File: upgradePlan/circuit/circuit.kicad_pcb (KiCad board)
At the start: 2 copper layers, 3 parts, among them U2 L293D, U3 LM317_TO-220, U5 LM317_TO-220

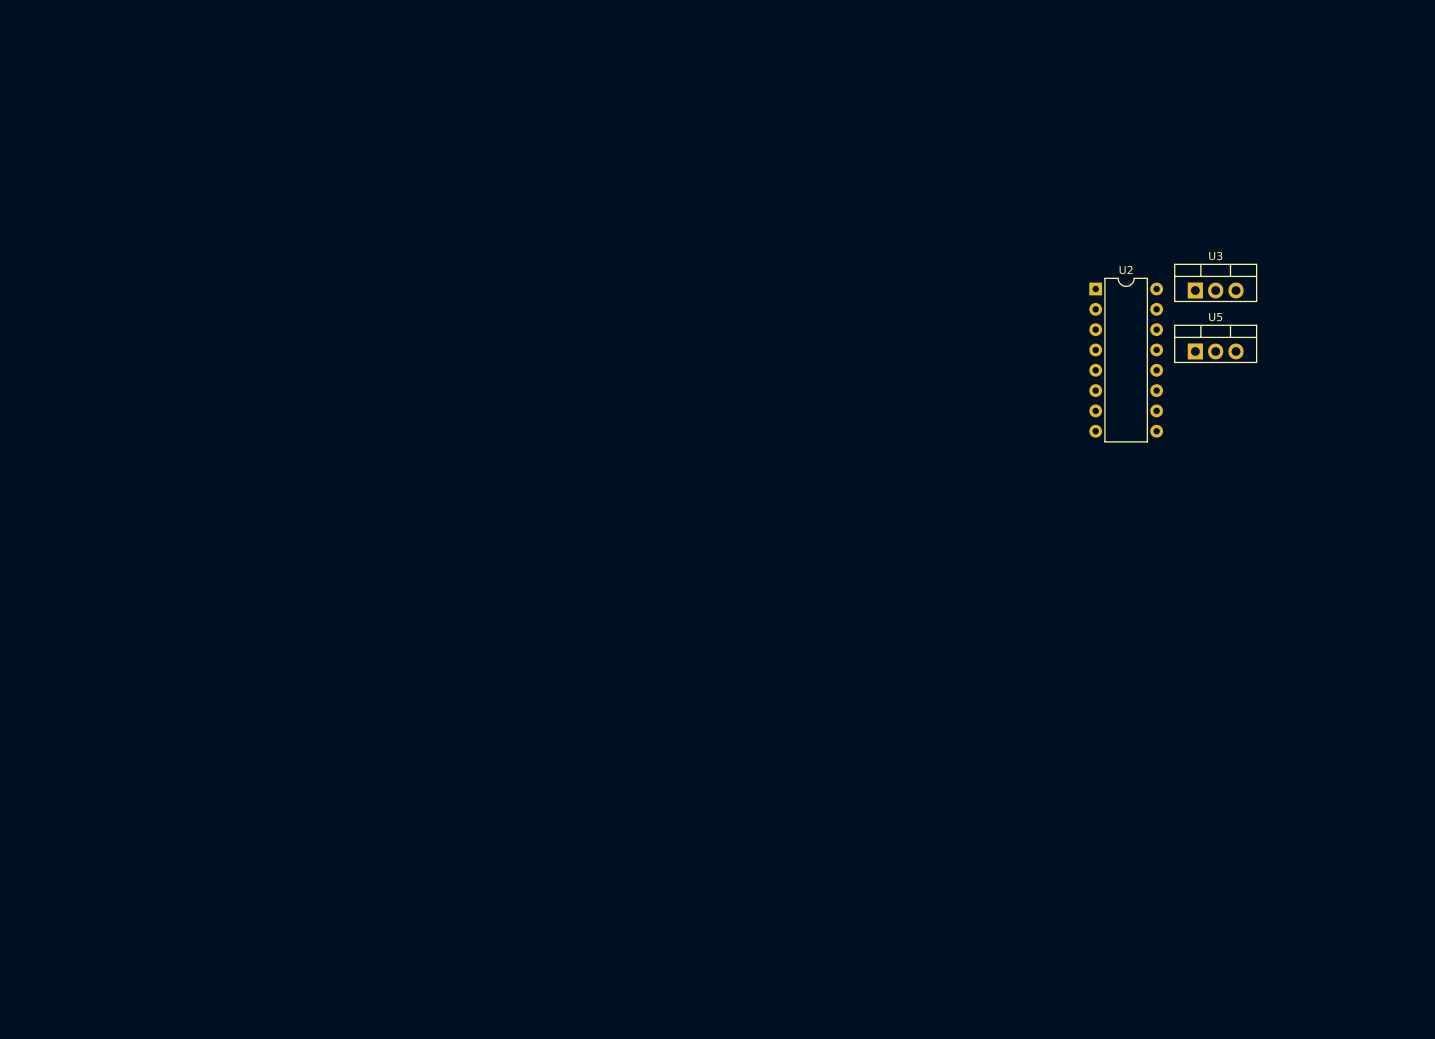
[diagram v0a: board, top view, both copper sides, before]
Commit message: added footprints to schematic and board edge
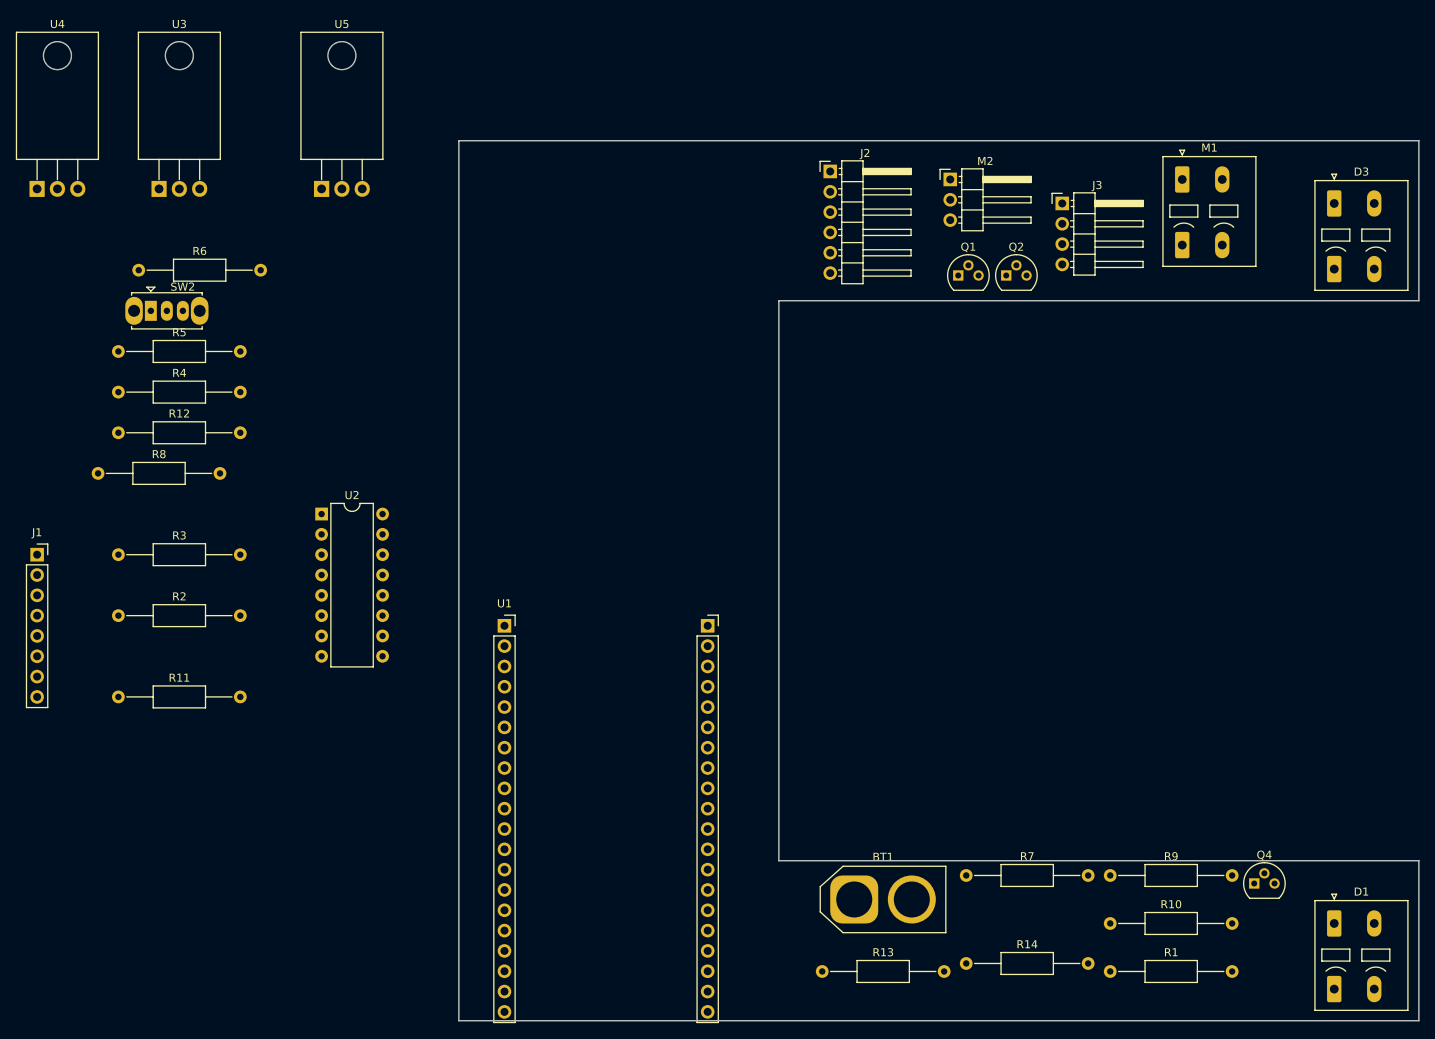
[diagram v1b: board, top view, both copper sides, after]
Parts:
- added BT1: Battery_Cell, Connector_AMASS:AMASS_XT60-M_1x02_P7.20mm_Vertical, F.Cu at (125.0, 132.0)
- added D1: LED, Connector_Phoenix_SPT:PhoenixContact_SPT_2.5_2-V-5.0-EX_1x02_P5.0mm_Vertical, F.Cu at (185.0, 135.0)
- added D3: LED, Connector_Phoenix_SPT:PhoenixContact_SPT_2.5_2-V-5.0-EX_1x02_P5.0mm_Vertical, F.Cu at (185.0, 45.0)
- added J1: Connector_GY_521, Connector_PinSocket_2.54mm:PinSocket_1x08_P2.54mm_Vertical, F.Cu at (22.9, 88.9)
- added J2: Conn_VL53L0/1xV2, Connector_PinHeader_2.54mm:PinHeader_1x06_P2.54mm_Horizontal, F.Cu at (122.0, 41.0)
- added J3: Conn_HC_SR04, Connector_PinHeader_2.54mm:PinHeader_1x04_P2.54mm_Horizontal, F.Cu at (151.0, 45.0)
- added M1: Motor_DC, Connector_Phoenix_SPT:PhoenixContact_SPT_2.5_2-V-5.0-EX_1x02_P5.0mm_Vertical, F.Cu at (166.0, 42.0)
- added M2: Motor_Servo, Connector_PinHeader_2.54mm:PinHeader_1x03_P2.54mm_Horizontal, F.Cu at (137.0, 42.0)
- added Q1: C945, Package_TO_SOT_THT:TO-92, F.Cu at (138.0, 54.0)
- added Q2: C945, Package_TO_SOT_THT:TO-92, F.Cu at (144.0, 54.0)
- added Q4: C945, Package_TO_SOT_THT:TO-92, F.Cu at (175.0, 130.0)
- added R1: 390, Resistor_THT:R_Axial_DIN0207_L6.3mm_D2.5mm_P15.24mm_Horizontal, F.Cu at (157.0, 141.0)
- added R10: 4k7, Resistor_THT:R_Axial_DIN0207_L6.3mm_D2.5mm_P15.24mm_Horizontal, F.Cu at (157.0, 135.0)
- added R11: 3k, Resistor_THT:R_Axial_DIN0207_L6.3mm_D2.5mm_P15.24mm_Horizontal, F.Cu at (33.0, 106.7)
- added R12: 100k, Resistor_THT:R_Axial_DIN0207_L6.3mm_D2.5mm_P15.24mm_Horizontal, F.Cu at (33.0, 73.7)
- added R13: 120, Resistor_THT:R_Axial_DIN0207_L6.3mm_D2.5mm_P15.24mm_Horizontal, F.Cu at (121.0, 141.0)
- added R14: 510, Resistor_THT:R_Axial_DIN0207_L6.3mm_D2.5mm_P15.24mm_Horizontal, F.Cu at (139.0, 140.0)
- added R2: 3k, Resistor_THT:R_Axial_DIN0207_L6.3mm_D2.5mm_P15.24mm_Horizontal, F.Cu at (33.0, 96.5)
- added R3: 220, Resistor_THT:R_Axial_DIN0207_L6.3mm_D2.5mm_P15.24mm_Horizontal, F.Cu at (33.0, 88.9)
- added R4: 220, Resistor_THT:R_Axial_DIN0207_L6.3mm_D2.5mm_P15.24mm_Horizontal, F.Cu at (33.0, 68.6)
- added R5: 1k, Resistor_THT:R_Axial_DIN0207_L6.3mm_D2.5mm_P15.24mm_Horizontal, F.Cu at (33.0, 63.5)
- added R6: 1k, Resistor_THT:R_Axial_DIN0207_L6.3mm_D2.5mm_P15.24mm_Horizontal, F.Cu at (35.6, 53.3)
- added R7: 39, Resistor_THT:R_Axial_DIN0207_L6.3mm_D2.5mm_P15.24mm_Horizontal, F.Cu at (139.0, 129.0)
- added R8: 120, Resistor_THT:R_Axial_DIN0207_L6.3mm_D2.5mm_P15.24mm_Horizontal, F.Cu at (30.5, 78.7)
- added R9: 4k7, Resistor_THT:R_Axial_DIN0207_L6.3mm_D2.5mm_P15.24mm_Horizontal, F.Cu at (157.0, 129.0)
- added SW2: SW_DPDT_x2, Button_Switch_THT:SW_Slide_1P2T_CK_OS102011MS2Q, F.Cu at (37.1, 58.4)
- added U1: Freenove-SP32-WROVER, MyESPConnector:MyESPConnector, F.Cu at (81.3, 97.8)
- added U4: LM350_TO220, Package_TO_SOT_THT:TO-220-3_Horizontal_TabDown, F.Cu at (22.9, 43.2)
- U3: value LM317_TO-220 -> LM350_TO220; footprint Package_TO_SOT_THT:TO-220-3_Vertical -> Package_TO_SOT_THT:TO-220-3_Horizontal_TabDown
- U5: footprint Package_TO_SOT_THT:TO-220-3_Vertical -> Package_TO_SOT_THT:TO-220-3_Horizontal_TabDown
- moved U3 130.2 mm to (38.1, 43.2)
- moved U5 111.1 mm to (58.4, 43.2)
- moved U2 100.8 mm to (58.4, 83.8)
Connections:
- U3 pad 3: Net-(U3-VI) -> /Drive Motor
- U5 pad 3: Net-(U3-VI) -> Net-(SW2A-B)
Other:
- board outline added: 120 x 110 mm

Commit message: added layout of footprints
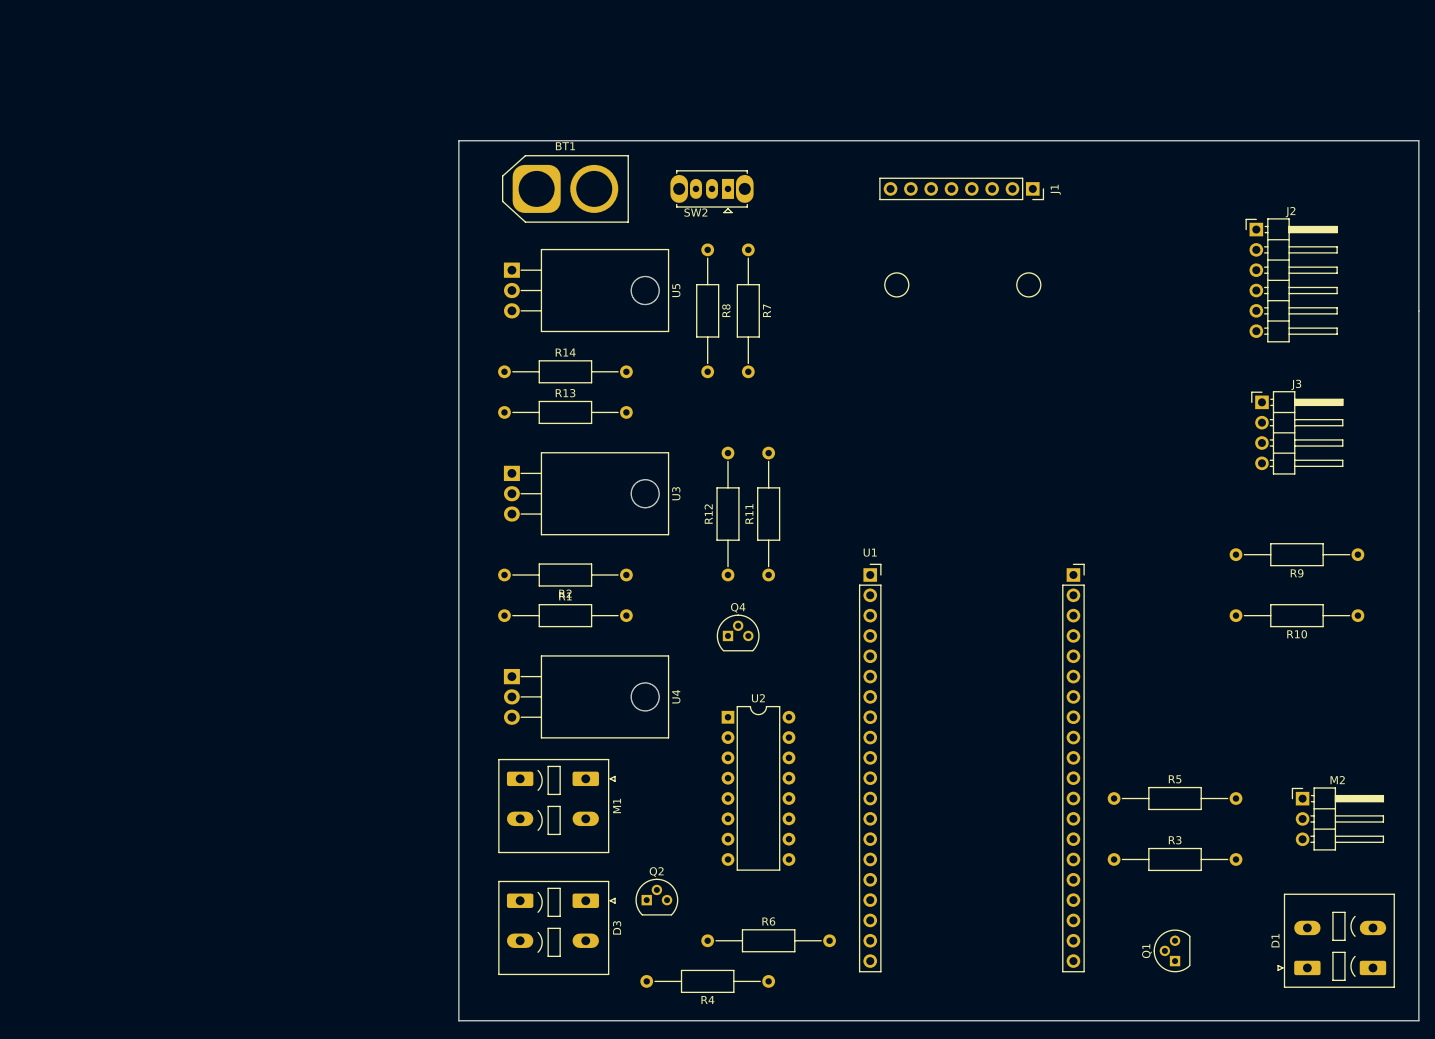
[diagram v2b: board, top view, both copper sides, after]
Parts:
- moved R5 136.4 mm to (157.5, 119.4)
- moved J1 132.6 mm to (147.3, 43.2), turned to -90 degrees
- moved R3 130.2 mm to (157.5, 127.0)
- moved D3 127.9 mm to (91.4, 132.2), turned to -90 degrees
- moved R6 109.9 mm to (106.7, 137.2)
- moved R4 109.7 mm to (114.3, 142.2), turned to 180 degrees
- moved M1 105.7 mm to (91.4, 116.9), turned to -90 degrees
- moved BT1 97.3 mm to (85.3, 43.2)
- moved R14 93.8 mm to (81.3, 66.0)
- moved Q2 90.1 mm to (99.1, 132.1)
- moved Q1 89.9 mm to (165.1, 139.7), turned to 90 degrees
- moved M2 89.1 mm to (181.0, 119.4)
- moved R1 87.8 mm to (81.3, 96.5)
- moved U4 85.1 mm to (82.2, 104.1), turned to -90 degrees
- moved R7 82.8 mm to (111.8, 50.8), turned to -90 degrees
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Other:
- outline, holes or cut-outs redrawn

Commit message: added front routing with auto completed back
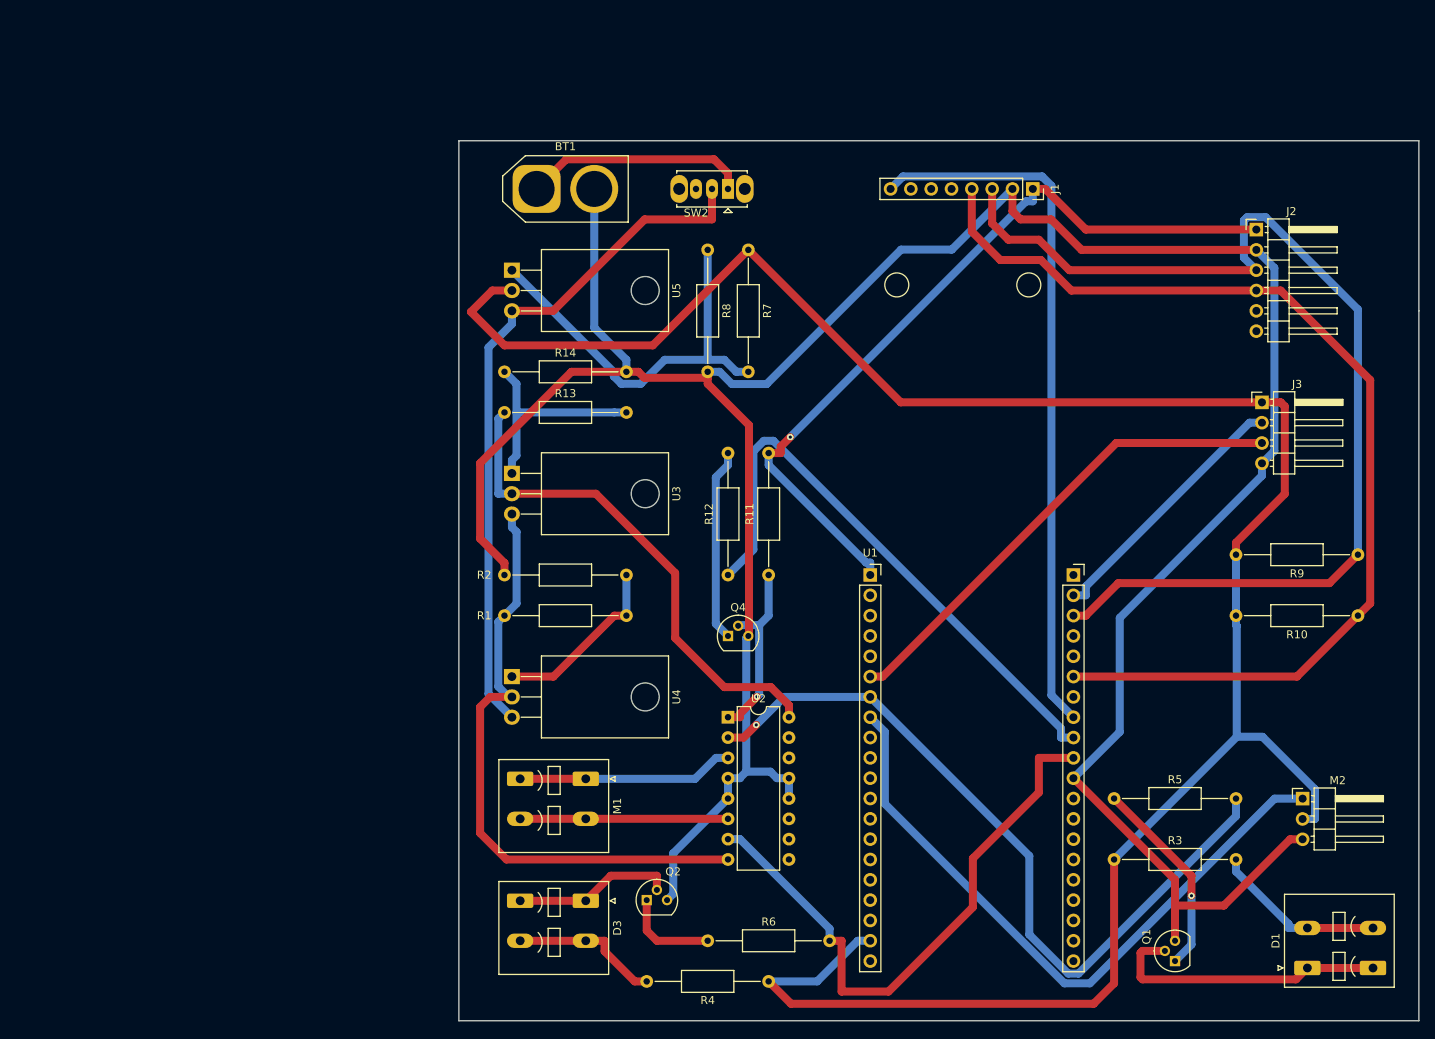
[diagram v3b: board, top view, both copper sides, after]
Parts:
- J1: footprint Connector_PinSocket_2.54mm:PinSocket_1x08_P2.54mm_Vertical -> MyESPConnector:GY-521
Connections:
- R1 pad 1: /Drive Motor -> /MotorDrive
- R13 pad 1: /Drive Motor -> /DriverPower
- U2 pad 12: unconnected-(U2-GND-Pad12) -> GND
- U2 pad 13: unconnected-(U2-GND-Pad13) -> GND
- U2 pad 16: /Drive Motor -> /DriverPower
- U2 pad 5: unconnected-(U2-GND-Pad5) -> GND
- U2 pad 8: /Drive Motor -> /MotorDrive
- U3 pad 2: /Drive Motor -> /DriverPower
- U3 pad 3: /Drive Motor -> /MotorDrive
- U4 pad 2: /Drive Motor -> /MotorDrive
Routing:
- net GND: track 0.00 -> 361.2 mm
- net /ESP Power: track 0.00 -> 281.7 mm
- net Net-(J1-SCL): track 0.00 -> 135.2 mm
- net Net-(J1-SDA): track 0.00 -> 131.6 mm
- net Net-(J1-VCC): track 0.00 -> 98.9 mm, vias 0 -> 1
- net Net-(U1-32): track 0.00 -> 96.0 mm, vias 0 -> 1
- net Net-(J1-INT): track 0.00 -> 88.8 mm
- net Net-(SW2A-B): track 0.00 -> 86.8 mm
- net Net-(M2-PWM): track 0.00 -> 82.7 mm
- net /MotorDrive: track 0.00 -> 77.6 mm
- net Net-(U1-5): track 0.00 -> 73.9 mm
- net Net-(U1-18): track 0.00 -> 73.4 mm
- net /DriverPower: track 0.00 -> 64.0 mm
- net Net-(J3-Echo): track 0.00 -> 61.1 mm
- net Net-(U5-ADJ): track 0.00 -> 51.3 mm
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
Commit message: Finished pcb Updated readme Generated Gerber files
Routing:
- net GND: track 361.2 -> 372.7 mm
- net Net-(M2-PWM): track 82.7 -> 91.1 mm
- net Net-(J1-INT): track 88.8 -> 96.2 mm
- net Net-(U1-32): track 96.0 -> 102.6 mm
- net Net-(J1-SCL): track 135.2 -> 141.0 mm
- net /ESP Power: track 281.7 -> 286.7 mm
- net Net-(U5-ADJ): track 51.3 -> 55.5 mm
- net Net-(SW2A-B): track 86.8 -> 89.4 mm
- net Net-(Q4-C): track 23.4 -> 25.9 mm
- net /MotorDrive: track 77.6 -> 80.0 mm
- net Net-(U1-18): track 73.4 -> 75.8 mm
- net Net-(Q1-B): track 25.2 -> 27.6 mm
- net /DriverPower: track 64.0 -> 65.8 mm
- net Net-(J1-VCC): track 98.9 -> 100.1 mm
- net Net-(Q4-B): track 24.1 -> 25.0 mm
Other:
- outline, holes or cut-outs redrawn
- board text added: "ESP-32"
- board text added: "IMU/Gyro/Accel"
- board text added: "ImpMotor"
- board text added: "LED"
- board text added: "ServoMotor"
- board text added: "ToF"
- board text added: "UltrSound"
